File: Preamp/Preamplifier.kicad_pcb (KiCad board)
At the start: 2 copper layers, 100 x 52 mm, 145 parts, among them J1 Conn_01x03_Male, J12 XLR3, J14 Conn_01x03, J15 Conn_01x02, J16 Conn_01x02, J17 Conn_01x02, J2 Conn_01x02_Male, J3 Conn_01x02_Male, J4 Conn_01x03_Male, J5 Conn_01x03_Male, J6 Conn_01x02_Male, J8 Conn_01x05_Female, J9 Conn_01x03, Q3 2N3904, Q4 2N3906, Q5 BC549, SW1 SW_HPF, SW2 SW_SPDT, SW3 GND LIFT, SW4 SW_SPST, SW5 SW_HPFQ, U1 OPA2134, U2 NE5532, U4 NE5532, U5 TL072, U6 NE5532, U7 NE5532, U8 NE5532, U9 NE5532

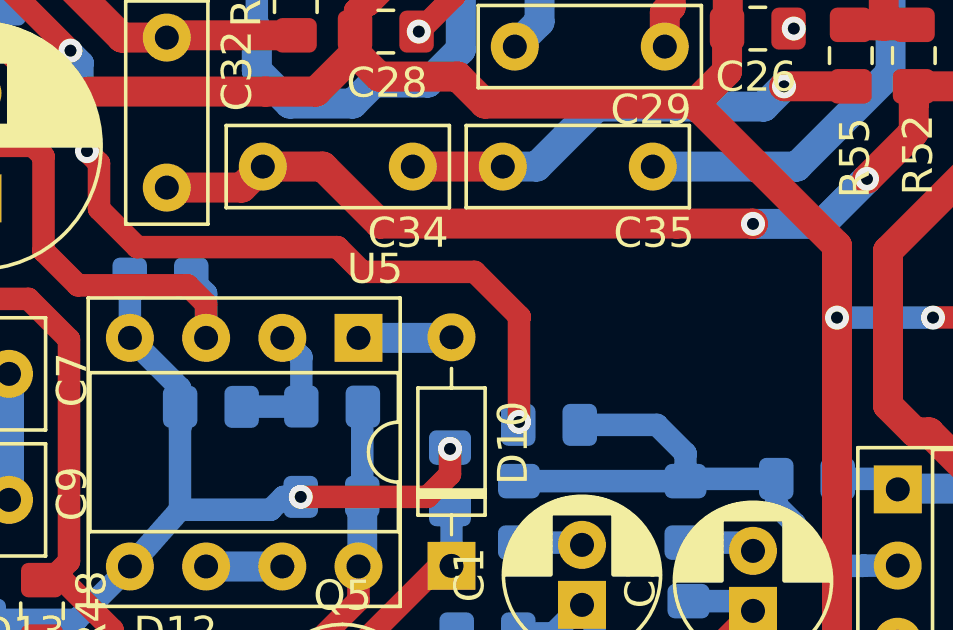
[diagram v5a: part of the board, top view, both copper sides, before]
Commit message: Added overload connector for EQ
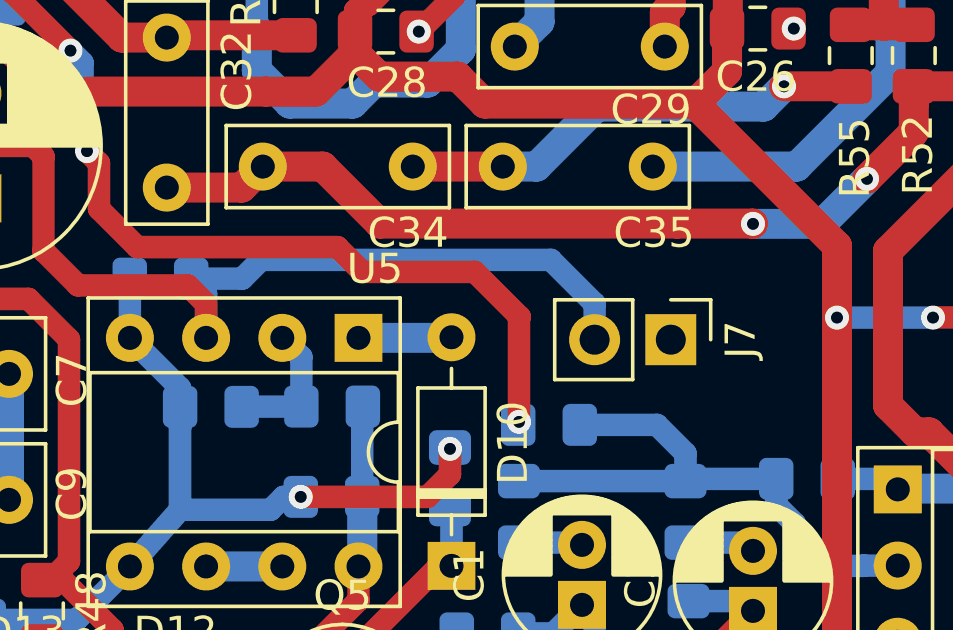
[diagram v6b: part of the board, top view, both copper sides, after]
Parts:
- added J7: Conn_01x02, Connector_PinHeader_2.54mm:PinHeader_1x02_P2.54mm_Vertical, F.Cu at (73.7, 84.8)
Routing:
- net Overload: track 34.4 -> 49.9 mm

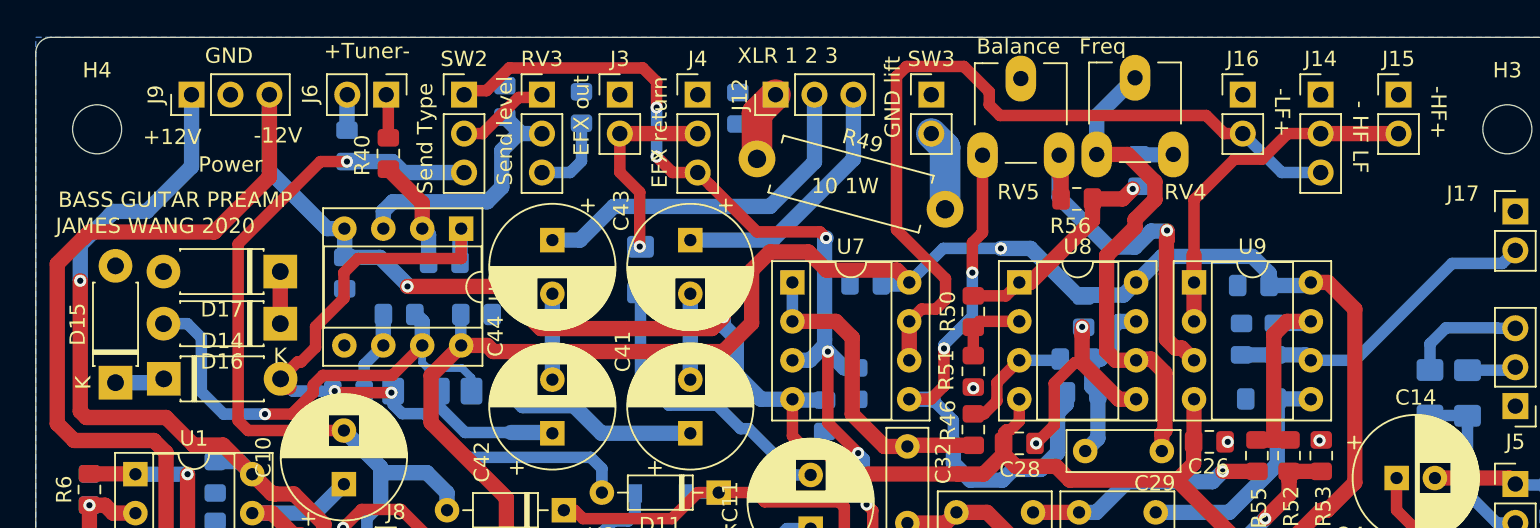
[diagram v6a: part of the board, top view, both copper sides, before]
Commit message: Added bulk caps, started eq board layout
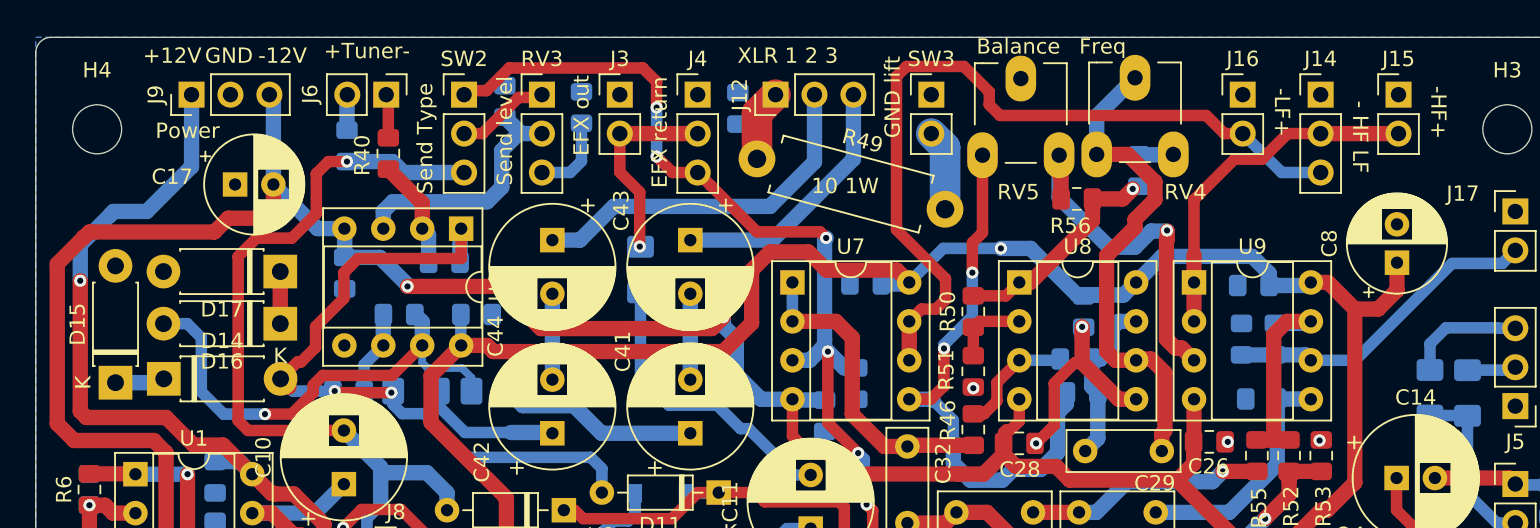
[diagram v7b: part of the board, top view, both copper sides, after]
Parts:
- added C17: 100uF 25V, Capacitor_THT:CP_Radial_D6.3mm_P2.50mm, F.Cu at (13.0, 57.6)
- added C8: 100uF 25V, Capacitor_THT:CP_Radial_D6.3mm_P2.50mm, F.Cu at (88.8, 62.7)
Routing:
- net +12V: track 251.3 -> 256.3 mm
- net -12V: track 210.4 -> 206.1 mm
- net PreEQ: track 70.0 -> 71.0 mm
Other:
- board text added: "Bass Guitar Preamp - James Wang 2020 (based off ESP Project 152)"
- board text removed: "BASS GUITAR PREAMP"
- board text removed: "JAMES WANG 2020"

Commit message: Finished first pass at Eq board
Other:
- board text added: "+Overload-"
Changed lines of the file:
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@@
   (general
     (thickness 1.6)
-    (drawings 41)
+    (drawings 42)
     (tracks 937)
     (zones 0)
@@
     )
   )
+  (gr_text +Overload- (at 72.3 82.1) (layer F.SilkS)
+    (effects (font (size 1 1) (thickness 0.25)))
+  )
   (gr_text "Bass Guitar Preamp - James Wang 2020 (based off ESP Project 152)" (at 27.6 49.1) (layer B.SilkS)
